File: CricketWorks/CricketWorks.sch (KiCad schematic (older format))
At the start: 10 parts, among them IC1 NE556N

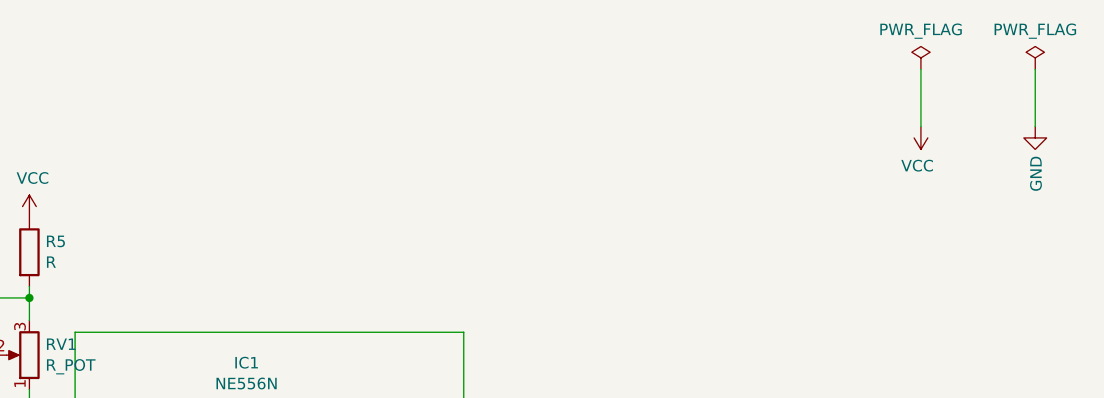
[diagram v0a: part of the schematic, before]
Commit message: added BioRuler initial commit
added project for a custom STM32 based solar powered ultracapacitor microcontroller for biological research
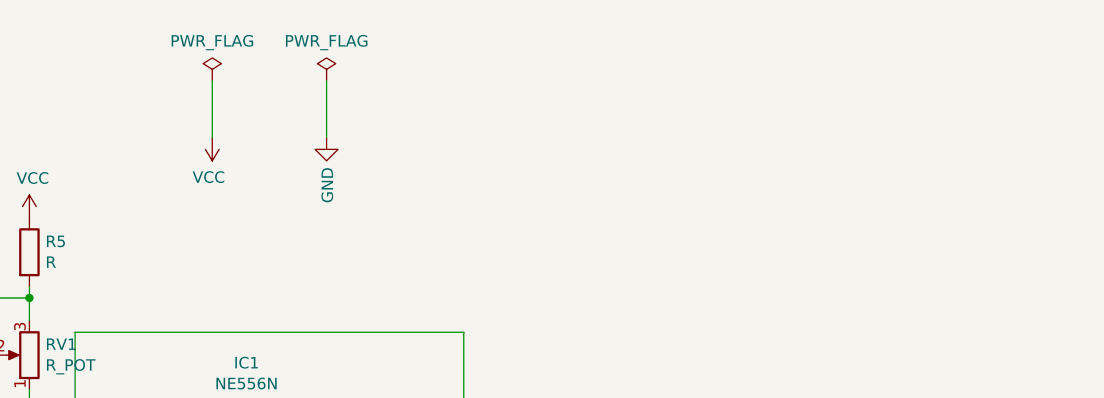
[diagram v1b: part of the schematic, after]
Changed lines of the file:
@@
 L power:PWR_FLAG #FLG0101
 U 1 1 6082430A
-P 8350 1500
-F 0 "#FLG0101" H 8350 1575 50  0001 C CNN
-F 1 "PWR_FLAG" H 8350 1673 50  0000 C CNN
-F 2 "" H 8350 1500 50  0001 C CNN
-F 3 "~" H 8350 1500 50  0001 C CNN
-	1    8350 1500
+P 5250 1550
+F 0 "#FLG0101" H 5250 1625 50  0001 C CNN
+F 1 "PWR_FLAG" H 5250 1723 50  0000 C CNN
+F 2 "" H 5250 1550 50  0001 C CNN
+F 3 "~" H 5250 1550 50  0001 C CNN
+	1    5250 1550
 	1    0    0    -1
 $EndComp
@@
 L power:PWR_FLAG #FLG0102
 U 1 1 60824721
-P 8850 1500
-F 0 "#FLG0102" H 8850 1575 50  0001 C CNN
-F 1 "PWR_FLAG" H 8850 1673 50  0000 C CNN
-F 2 "" H 8850 1500 50  0001 C CNN
-F 3 "~" H 8850 1500 50  0001 C CNN
-	1    8850 1500
+P 5750 1550
+F 0 "#FLG0102" H 5750 1625 50  0001 C CNN
+F 1 "PWR_FLAG" H 5750 1723 50  0000 C CNN
+F 2 "" H 5750 1550 50  0001 C CNN
+F 3 "~" H 5750 1550 50  0001 C CNN
+	1    5750 1550
 	1    0    0    -1
 $EndComp
@@
 L power:VCC #PWR0103
 U 1 1 60824AE0
-P 8350 1750
-F 0 "#PWR0103" H 8350 1600 50  0001 C CNN
-F 1 "VCC" H 8365 1923 50  0000 C CNN
-F 2 "" H 8350 1750 50  0001 C CNN
-F 3 "" H 8350 1750 50  0001 C CNN
-	1    8350 1750
+P 5250 1800
+F 0 "#PWR0103" H 5250 1650 50  0001 C CNN
+F 1 "VCC" H 5265 1973 50  0000 C CNN
+F 2 "" H 5250 1800 50  0001 C CNN
+F 3 "" H 5250 1800 50  0001 C CNN
+	1    5250 1800
 	-1   0    0    1
 $EndComp
@@
 L power:GND #PWR0104
 U 1 1 608252A3
-P 8850 1750
-F 0 "#PWR0104" H 8850 1500 50  0001 C CNN
-F 1 "GND" V 8855 1622 50  0000 R CNN
-F 2 "" H 8850 1750 50  0001 C CNN
-F 3 "" H 8850 1750 50  0001 C CNN
-	1    8850 1750
+P 5750 1800
+F 0 "#PWR0104" H 5750 1550 50  0001 C CNN
+F 1 "GND" V 5755 1672 50  0000 R CNN
+F 2 "" H 5750 1800 50  0001 C CNN
+F 3 "" H 5750 1800 50  0001 C CNN
+	1    5750 1800
 	1    0    0    -1
 $EndComp
 Wire Wire Line
-	8850 1750 8850 1500
+	5750 1800 5750 1550
 Wire Wire Line
-	8350 1750 8350 1500
+	5250 1800 5250 1550
 Wire Wire Line
 	4450 2500 4150 2500
